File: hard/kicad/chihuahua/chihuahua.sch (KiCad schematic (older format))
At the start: 36 parts, among them J1 CARTRIDGE, J2 VIAport, J3 IOx, J4 nanoLink, J5 STEP, J6 POWER, Q1 BC548, Q2 BC548, SW1 RESET, SW2 NMI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

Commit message: mostly routed Chihuahua
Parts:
- JP4: value CA1L -> LATCH; footprint Connector_PinHeader_2.54mm:PinHeader_1x02_P2.54mm_Horizontal -> Connector_PinHeader_2.54mm:PinHeader_1x02_P2.54mm_Vertical
- R3, R4: value R -> 3K3
- R5: value R -> 1K
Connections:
- net +5V: now also SW1.2; no longer SW1.1
- net A15: now also U4.9; no longer U4.12
- net CB2: now also U5.1, U5.2, U5.3, U5.4, U5.5, U5.6; no longer U5.10, U5.11, U5.12, U5.13, U5.8, U5.9
- net PB7: now also U5.10, U5.8, U5.9; no longer U5.4, U5.5, U5.6
- net PHI1: now also U5.13; no longer U5.2
- net ROM_~CS: now also U4.8; no longer U4.11
- net ROM_~OE: now also U4.11; no longer U4.8
- net R~W: now also U4.12, U5.12; no longer U4.9, U5.1
- net U_RST: now also SW1.1; no longer SW1.2
- net VIA_~CS: now also U4.13; no longer U4.10
- net ~IOC: now also U4.10; no longer U4.13
- net ~WE: now also U5.11; no longer U5.3
- net ~VP: now reaches JP3.1 (A), U1.1 (~VP)
- net VIA_~IRQ renamed ~VREQ
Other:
- moved on the sheet: U4C, U4D, U5A, U5B, U5C, U5D
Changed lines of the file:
@@
 U 1 1 6526D457
 P 4750 1200
-F 0 "SW1" V 4400 1200 50  0000 C CNN
-F 1 "RESET" V 4500 1200 50  0000 C CNN
+F 0 "SW1" V 5000 1200 50  0000 C CNN
+F 1 "RESET" V 4800 1400 50  0000 C CNN
 F 2 "Button_Switch_THT:SW_PUSH_6mm" H 4750 1400 50  0001 C CNN
 F 3 "~" H 4750 1400 50  0001 C CNN
 	1    4750 1200
-	0    1    1    0
+	0    1    -1   0
 $EndComp
 $Comp
@@
 U 1 1 6526DC44
 P 2900 1200
-F 0 "SW2" V 3250 1200 50  0000 C CNN
-F 1 "NMI" V 3150 1200 50  0000 C CNN
+F 0 "SW2" V 3150 1200 50  0000 C CNN
+F 1 "NMI" V 3000 1350 50  0000 C CNN
 F 2 "Button_Switch_THT:SW_PUSH_6mm" H 2900 1400 50  0001 C CNN
 F 3 "~" H 2900 1400 50  0001 C CNN
@@
 P 4900 1500
 F 0 "R3" V 5000 1450 50  0000 L CNN
-F 1 "R" V 4900 1500 50  0000 L CNN
+F 1 "3K3" V 4900 1500 50  0000 C CNN
 F 2 "Resistor_THT:R_Axial_DIN0207_L6.3mm_D2.5mm_P2.54mm_Vertical" V 4830 1500 50  0001 C CNN
 F 3 "~" H 4900 1500 50  0001 C CNN
@@
 L 74xx:74LS132 U4
 U 4 1 652F182D
-P 8600 5100
-F 0 "U4" H 8600 5425 50  0000 C CNN
-F 1 "74HC132" H 8600 5334 50  0000 C CNN
-F 2 "Package_DIP:DIP-14_W7.62mm_Socket" H 8600 5100 50  0001 C CNN
-F 3 "http://www.ti.com/lit/gpn/sn74LS132" H 8600 5100 50  0001 C CNN
-	4    8600 5100
+P 8600 5800
+F 0 "U4" H 8600 6125 50  0000 C CNN
+F 1 "74HC132" H 8600 6034 50  0000 C CNN
+F 2 "Package_DIP:DIP-14_W7.62mm_Socket" H 8600 5800 50  0001 C CNN
+F 3 "http://www.ti.com/lit/gpn/sn74LS132" H 8600 5800 50  0001 C CNN
+	4    8600 5800
 	1    0    0    -1
 $EndComp
@@
 L 74xx:74LS32 U5
 U 1 1 652F4B6D
+P 1450 6450
+F 0 "U5" H 1450 6775 50  0000 C CNN
+F 1 "74HC32" H 1450 6684 50  0000 C CNN
+F 2 "Package_DIP:DIP-14_W7.62mm_Socket" H 1450 6450 50  0001 C CNN
+F 3 "http://www.ti.com/lit/gpn/sn74LS32" H 1450 6450 50  0001 C CNN
+	1    1450 6450
+	-1   0    0    -1
+$EndComp
+$Comp
+L 74xx:74LS32 U5
+U 2 1 652F645B
+P 1450 5900
+F 0 "U5" H 1450 6225 50  0000 C CNN
+F 1 "74HC32" H 1450 6134 50  0000 C CNN
+F 2 "Package_DIP:DIP-14_W7.62mm_Socket" H 1450 5900 50  0001 C CNN
+F 3 "http://www.ti.com/lit/gpn/sn74LS32" H 1450 5900 50  0001 C CNN
+	2    1450 5900
+	-1   0    0    -1
+$EndComp
+$Comp
+L 74xx:74LS32 U5
+U 3 1 652F75F5
+P 1800 7350
+F 0 "U5" H 1800 7675 50  0000 C CNN
+F 1 "74HC32" H 1800 7584 50  0000 C CNN
+F 2 "Package_DIP:DIP-14_W7.62mm_Socket" H 1800 7350 50  0001 C CNN
+F 3 "http://www.ti.com/lit/gpn/sn74LS32" H 1800 7350 50  0001 C CNN
+	3    1800 7350
+	-1   0    0    -1
+$EndComp
+$Comp
+L 74xx:74LS32 U5
+U 4 1 652F888B
 P 5700 5500
 F 0 "U5" H 5700 5825 50  0000 C CNN
@@
 F 2 "Package_DIP:DIP-14_W7.62mm_Socket" H 5700 5500 50  0001 C CNN
 F 3 "http://www.ti.com/lit/gpn/sn74LS32" H 5700 5500 50  0001 C CNN
-	1    5700 5500
-	1    0    0    -1
-$EndComp
-$Comp
-L 74xx:74LS32 U5
-U 2 1 652F645B
-P 1800 7350
-F 0 "U5" H 1800 7675 50  0000 C CNN
-F 1 "74HC32" H 1800 7584 50  0000 C CNN
-F 2 "Package_DIP:DIP-14_W7.62mm_Socket" H 1800 7350 50  0001 C CNN
-F 3 "http://www.ti.com/lit/gpn/sn74LS32" H 1800 7350 50  0001 C CNN
-	2    1800 7350
-	-1   0    0    -1
-$EndComp
-$Comp
-L 74xx:74LS32 U5
-U 3 1 652F75F5
-P 1450 5900
-F 0 "U5" H 1450 6225 50  0000 C CNN
-F 1 "74HC32" H 1450 6134 50  0000 C CNN
-F 2 "Package_DIP:DIP-14_W7.62mm_Socket" H 1450 5900 50  0001 C CNN
-F 3 "http://www.ti.com/lit/gpn/sn74LS32" H 1450 5900 50  0001 C CNN
-	3    1450 5900
-	-1   0    0    -1
-$EndComp
-$Comp
-L 74xx:74LS32 U5
-U 4 1 652F888B
-P 1450 6450
-F 0 "U5" H 1450 6775 50  0000 C CNN
-F 1 "74HC32" H 1450 6684 50  0000 C CNN
-F 2 "Package_DIP:DIP-14_W7.62mm_Socket" H 1450 6450 50  0001 C CNN
-F 3 "http://www.ti.com/lit/gpn/sn74LS32" H 1450 6450 50  0001 C CNN
-	4    1450 6450
-	-1   0    0    -1
+	4    5700 5500
+	1    0    0    -1
 $EndComp
 $Comp
@@
 P 2750 1500
 F 0 "R4" V 2850 1450 50  0000 L CNN
-F 1 "R" V 2750 1450 50  0000 L CNN
+F 1 "3K3" V 2750 1500 50  0000 C CNN
 F 2 "Resistor_THT:R_Axial_DIN0207_L6.3mm_D2.5mm_P2.54mm_Vertical" V 2680 1500 50  0001 C CNN
 F 3 "~" H 2750 1500 50  0001 C CNN
@@
 A3
 Text Label 3400 4150 3    50   ~ 0
-VIA_~IRQ
+~VREQ
 Text Label 3350 3950 0    50   ~ 0
 SCLK
@@
 L 74xx:74LS132 U4
 U 3 1 652EF95C
-P 8600 5800
-F 0 "U4" H 8600 6125 50  0000 C CNN
-F 1 "74HC132" H 8600 6034 50  0000 C CNN
-F 2 "Package_DIP:DIP-14_W7.62mm_Socket" H 8600 5800 50  0001 C CNN
-F 3 "http://www.ti.com/lit/gpn/sn74LS132" H 8600 5800 50  0001 C CNN
-	3    8600 5800
+P 8600 5100
+F 0 "U4" H 8600 5425 50  0000 C CNN
+F 1 "74HC132" H 8600 5334 50  0000 C CNN
+F 2 "Package_DIP:DIP-14_W7.62mm_Socket" H 8600 5100 50  0001 C CNN
+F 3 "http://www.ti.com/lit/gpn/sn74LS132" H 8600 5100 50  0001 C CNN
+	3    8600 5100
 	1    0    0    -1
 $EndComp
@@
 P 5900 6600
 F 0 "R5" H 5970 6646 50  0000 L CNN
-F 1 "R" V 5900 6550 50  0000 L CNN
+F 1 "1K" V 5900 6550 50  0000 L CNN
 F 2 "Resistor_THT:R_Axial_DIN0207_L6.3mm_D2.5mm_P2.54mm_Vertical" V 5830 6600 50  0001 C CNN
 F 3 "~" H 5900 6600 50  0001 C CNN
@@
 P 1950 3350
 F 0 "JP4" V 1850 3400 50  0000 L CNN
-F 1 "CA1L" V 1950 3150 50  0000 L CNN
-F 2 "Connector_PinHeader_2.54mm:PinHeader_1x02_P2.54mm_Horizontal" H 1950 3350 50  0001 C CNN
+F 1 "LATCH" V 1850 3100 50  0000 L CNN
+F 2 "Connector_PinHeader_2.54mm:PinHeader_1x02_P2.54mm_Vertical" H 1950 3350 50  0001 C CNN
 F 3 "~" H 1950 3350 50  0001 C CNN
 	1    1950 3350
@@
 Wire Bus Line
 	7500 1600 7500 3750
+Text Label 4500 4750 2    50   ~ 0
+~VP
 $EndSCHEMATC

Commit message: finish silkscreen, not sure about /IOC
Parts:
- added LOGO1: Logo_Open_Hardware_Large, Symbol:OSHW-Symbol_8.9x8mm_SilkScreen, symbol Graphic:Logo_Open_Hardware_Large
- added LOGO2: Logo_Open_Hardware_Small, durango:jaqueria, symbol Graphic:Logo_Open_Hardware_Small
- D1: footprint Diode_THT:D_DO-35_SOD27_P2.54mm_Vertical_AnodeUp -> Diode_THT:D_DO-35_SOD27_P2.54mm_Vertical_KathodeUp
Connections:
- net ~IOC is gone; now on net PB5: J1.4 (Pin_4), U4.10
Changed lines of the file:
@@
 F 0 "D1" H 3550 4250 50  0000 C CNN
 F 1 "BAT85" H 3550 4050 50  0000 C CNN
-F 2 "Diode_THT:D_DO-35_SOD27_P2.54mm_Vertical_AnodeUp" H 3550 4150 50  0001 C CNN
+F 2 "Diode_THT:D_DO-35_SOD27_P2.54mm_Vertical_KathodeUp" H 3550 4150 50  0001 C CNN
 F 3 "~" H 3550 4150 50  0001 C CNN
 	1    3550 4150
@@
 	750  5150 1050 5150
 Wire Wire Line
-	1050 5250 750  5250
+	1050 5250 800  5250
 Wire Wire Line
 	750  5350 1050 5350
@@
 Wire Wire Line
 	1950 3050 2350 3050
-Wire Bus Line
-	3650 1600 5600 1600
-Wire Bus Line
-	800  1800 800  2500
-Wire Bus Line
-	3650 1600 3650 3250
-Wire Bus Line
-	9100 3950 9100 4450
-Wire Bus Line
-	1950 3550 1950 4250
-Wire Bus Line
-	1950 1800 1950 2750
-Wire Bus Line
-	3550 1700 3550 2750
-Wire Bus Line
-	4000 1700 4000 2750
-Wire Bus Line
-	650  4250 650  5350
-Wire Bus Line
-	650  1000 650  4250
-Wire Bus Line
-	1950 900  1950 1800
-Wire Bus Line
-	5600 1600 5600 3550
-Wire Bus Line
-	7400 1700 7400 4450
-Wire Bus Line
-	7500 1600 7500 3750
 Text Label 4500 4750 2    50   ~ 0
 ~VP
+$Comp
+L Graphic:Logo_Open_Hardware_Large LOGO1
+U 1 1 65300219
+P 10200 3600
+F 0 "LOGO1" H 10200 4100 50  0001 C CNN
+F 1 "Logo_Open_Hardware_Large" H 10200 3200 50  0001 C CNN
+F 2 "Symbol:OSHW-Symbol_8.9x8mm_SilkScreen" H 10200 3600 50  0001 C CNN
+F 3 "~" H 10200 3600 50  0001 C CNN
+	1    10200 3600
+	1    0    0    -1
+$EndComp
+$Comp
+L Graphic:Logo_Open_Hardware_Small LOGO2
+U 1 1 65301B9B
+P 10200 4950
+F 0 "LOGO2" H 10200 5225 50  0001 C CNN
+F 1 "Logo_Open_Hardware_Small" H 10200 4725 50  0001 C CNN
+F 2 "durango:jaqueria" H 10200 4950 50  0001 C CNN
+F 3 "~" H 10200 4950 50  0001 C CNN
+	1    10200 4950
+	1    0    0    -1
+$EndComp
+Wire Wire Line
+	800  5250 800  5600
+Wire Bus Line
+	3650 1600 5600 1600
+Wire Bus Line
+	800  1800 800  2500
+Wire Bus Line
+	3650 1600 3650 3250
+Wire Bus Line
+	9100 3950 9100 4450
+Wire Bus Line
+	1950 3550 1950 4250
+Wire Bus Line
+	1950 1800 1950 2750
+Wire Bus Line
+	3550 1700 3550 2750
+Wire Bus Line
+	4000 1700 4000 2750
+Wire Bus Line
+	650  4250 650  5350
+Wire Bus Line
+	650  1000 650  4250
+Wire Bus Line
+	1950 900  1950 1800
+Wire Bus Line
+	5600 1600 5600 3550
+Wire Bus Line
+	7400 1700 7400 4450
+Wire Bus Line
+	7500 1600 7500 3750
+Connection ~ 800  5250
+Wire Wire Line
+	800  5250 750  5250
+Text Label 800  5600 0    50   ~ 0
+~IOC
 $EndSCHEMATC

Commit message: completely remove /IOC from Chihuahua
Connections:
- net +5V: now also J1.4 (Pin_4), U4.10
- net PB5: no longer J1.4 (Pin_4), U4.10
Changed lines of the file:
@@
 	750  5150 1050 5150
-Wire Wire Line
-	1050 5250 800  5250
 Wire Wire Line
 	750  5350 1050 5350
@@
 	1    0    0    -1
 $EndComp
-Wire Wire Line
-	800  5250 800  5600
 Wire Bus Line
 	3650 1600 5600 1600
@@
 Wire Bus Line
 	7500 1600 7500 3750
-Connection ~ 800  5250
 Wire Wire Line
-	800  5250 750  5250
-Text Label 800  5600 0    50   ~ 0
-~IOC
+	750  5250 1050 5250
+$Comp
+L power:+5V #PWR?
+U 1 1 652EE0F4
+P 9300 5350
+F 0 "#PWR?" H 9300 5200 50  0001 C CNN
+F 1 "+5V" V 9315 5478 50  0000 L CNN
+F 2 "" H 9300 5350 50  0001 C CNN
+F 3 "" H 9300 5350 50  0001 C CNN
+	1    9300 5350
+	0    1    1    0
+$EndComp
+Connection ~ 9300 5350
 $EndSCHEMATC

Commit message: fix R/W label
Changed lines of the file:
@@
 $EndComp
 Text Label 8300 5700 2    50   ~ 0
-~RW
+R~W
 Text Label 8300 5900 2    50   ~ 0
 VIA_~CS
@@
 	1    0    0    -1
 $EndComp
-Wire Bus Line
-	3650 1600 5600 1600
-Wire Bus Line
-	800  1800 800  2500
-Wire Bus Line
-	3650 1600 3650 3250
-Wire Bus Line
-	9100 3950 9100 4450
-Wire Bus Line
-	1950 3550 1950 4250
-Wire Bus Line
-	1950 1800 1950 2750
-Wire Bus Line
-	3550 1700 3550 2750
-Wire Bus Line
-	4000 1700 4000 2750
-Wire Bus Line
-	650  4250 650  5350
-Wire Bus Line
-	650  1000 650  4250
-Wire Bus Line
-	1950 900  1950 1800
-Wire Bus Line
-	5600 1600 5600 3550
-Wire Bus Line
-	7400 1700 7400 4450
-Wire Bus Line
-	7500 1600 7500 3750
 Wire Wire Line
 	750  5250 1050 5250
@@
 $EndComp
 Connection ~ 9300 5350
+Wire Bus Line
+	3650 1600 5600 1600
+Wire Bus Line
+	800  1800 800  2500
+Wire Bus Line
+	3650 1600 3650 3250
+Wire Bus Line
+	9100 3950 9100 4450
+Wire Bus Line
+	1950 3550 1950 4250
+Wire Bus Line
+	1950 1800 1950 2750
+Wire Bus Line
+	3550 1700 3550 2750
+Wire Bus Line
+	4000 1700 4000 2750
+Wire Bus Line
+	650  4250 650  5350
+Wire Bus Line
+	650  1000 650  4250
+Wire Bus Line
+	1950 900  1950 1800
+Wire Bus Line
+	5600 1600 5600 3550
+Wire Bus Line
+	7400 1700 7400 4450
+Wire Bus Line
+	7500 1600 7500 3750
 $EndSCHEMATC

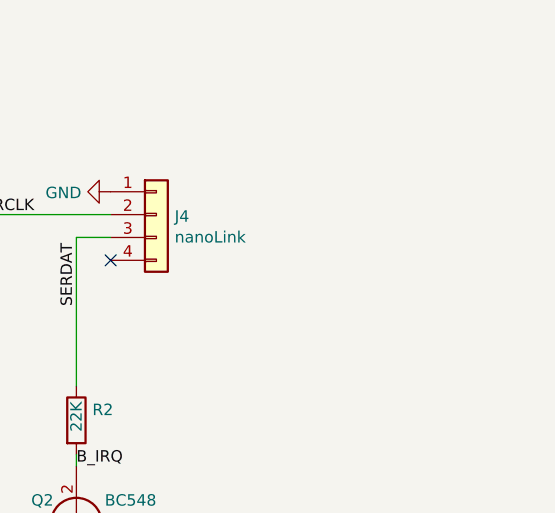
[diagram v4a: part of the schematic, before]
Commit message: add holes and thicken tracks
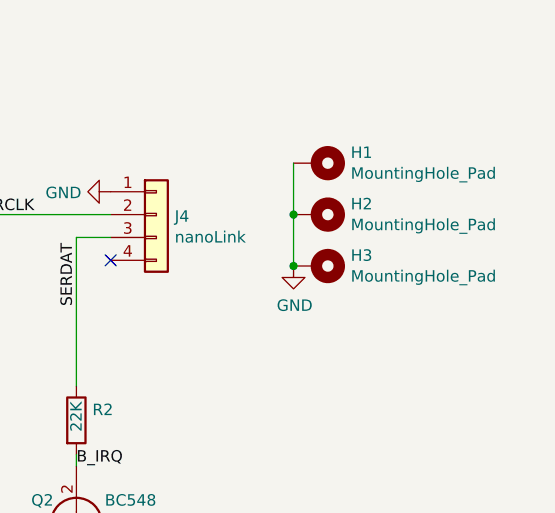
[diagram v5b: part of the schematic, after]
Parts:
- added H1, H2, H3: MountingHole_Pad, MountingHole:MountingHole_3.2mm_M3_DIN965_Pad, symbol Mechanical:MountingHole_Pad
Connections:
- net GND: now also H1.1, H2.1, H3.1
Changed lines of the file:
@@
 	750  5250 1050 5250
 $Comp
-L power:+5V #PWR?
+L power:+5V #PWR0131
 U 1 1 652EE0F4
 P 9300 5350
-F 0 "#PWR?" H 9300 5200 50  0001 C CNN
+F 0 "#PWR0131" H 9300 5200 50  0001 C CNN
 F 1 "+5V" V 9315 5478 50  0000 L CNN
 F 2 "" H 9300 5350 50  0001 C CNN
@@
 $EndComp
 Connection ~ 9300 5350
+$Comp
+L Mechanical:MountingHole_Pad H1
+U 1 1 65AE728F
+P 10250 1025
+F 0 "H1" V 10204 1175 50  0000 L CNN
+F 1 "MountingHole_Pad" V 10295 1175 50  0000 L CNN
+F 2 "MountingHole:MountingHole_3.2mm_M3_DIN965_Pad" H 10250 1025 50  0001 C CNN
+F 3 "~" H 10250 1025 50  0001 C CNN
+	1    10250 1025
+	0    1    1    0
+$EndComp
+$Comp
+L Mechanical:MountingHole_Pad H2
+U 1 1 65AE7CE7
+P 10250 1250
+F 0 "H2" V 10204 1400 50  0000 L CNN
+F 1 "MountingHole_Pad" V 10295 1400 50  0000 L CNN
+F 2 "MountingHole:MountingHole_3.2mm_M3_DIN965_Pad" H 10250 1250 50  0001 C CNN
+F 3 "~" H 10250 1250 50  0001 C CNN
+	1    10250 1250
+	0    1    1    0
+$EndComp
+$Comp
+L Mechanical:MountingHole_Pad H3
+U 1 1 65AE8CBA
+P 10250 1475
+F 0 "H3" V 10204 1625 50  0000 L CNN
+F 1 "MountingHole_Pad" V 10295 1625 50  0000 L CNN
+F 2 "MountingHole:MountingHole_3.2mm_M3_DIN965_Pad" H 10250 1475 50  0001 C CNN
+F 3 "~" H 10250 1475 50  0001 C CNN
+	1    10250 1475
+	0    1    1    0
+$EndComp
+Wire Wire Line
+	10150 1025 10150 1250
+Connection ~ 10150 1250
+Wire Wire Line
+	10150 1250 10150 1475
+$Comp
+L power:GND #PWR0132
+U 1 1 65B0B18F
+P 10150 1475
+F 0 "#PWR0132" H 10150 1225 50  0001 C CNN
+F 1 "GND" H 10155 1302 50  0000 C CNN
+F 2 "" H 10150 1475 50  0001 C CNN
+F 3 "" H 10150 1475 50  0001 C CNN
+	1    10150 1475
+	1    0    0    -1
+$EndComp
+Connection ~ 10150 1475
 Wire Bus Line
 	3650 1600 5600 1600
